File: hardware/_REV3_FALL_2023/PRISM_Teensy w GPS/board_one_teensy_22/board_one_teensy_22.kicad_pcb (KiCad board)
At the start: 2 copper layers, 61 x 88.9 mm, 32 parts, among them J1 Micro_SD_Card_Det_Hirose_DM3AT, J3 3387, Q1 AO3400A, Q2 AO3400A, U1 Teensy4.0, U2 GPS-14414, U3 3966, U4 RFM69HCW_Breakout, U5 CT25E-16T150-1, U6 CMI-9605-1280T

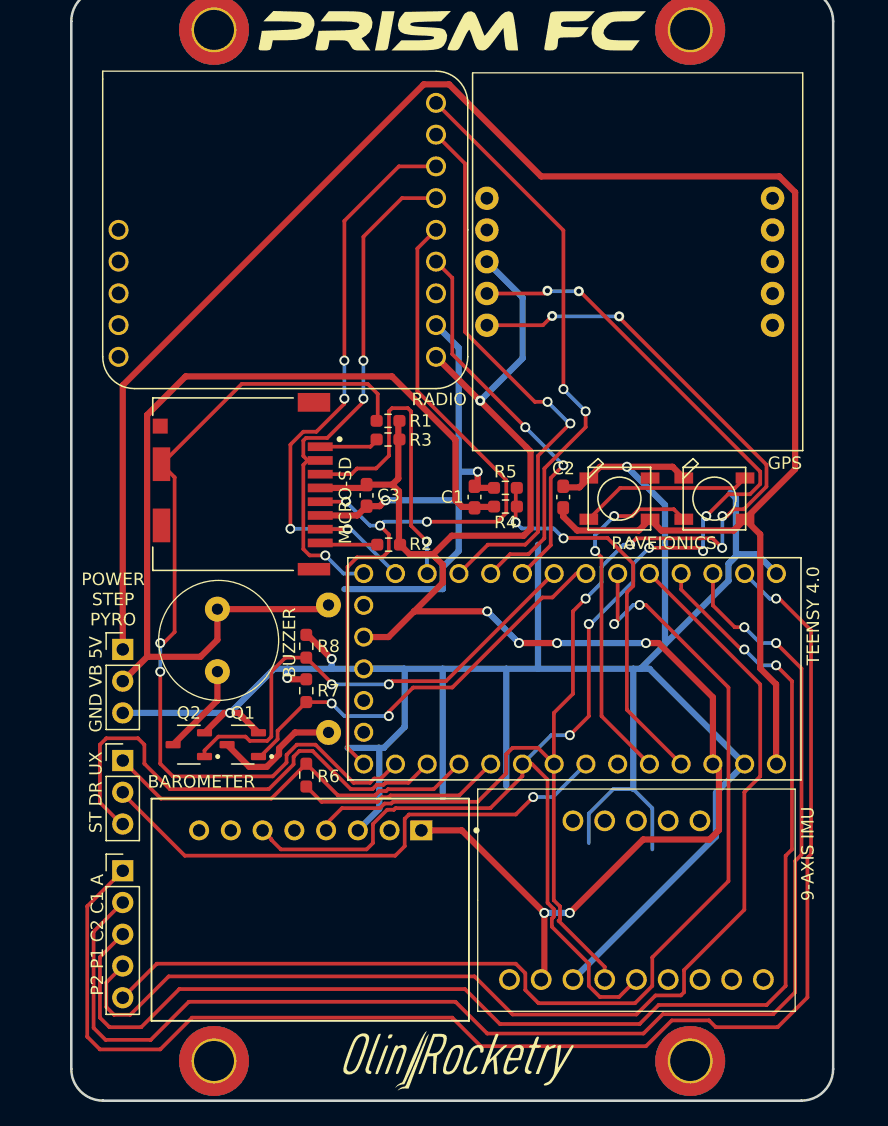
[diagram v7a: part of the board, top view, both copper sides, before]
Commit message: Added 3.3V line and fixed analog routing issues on Teensy
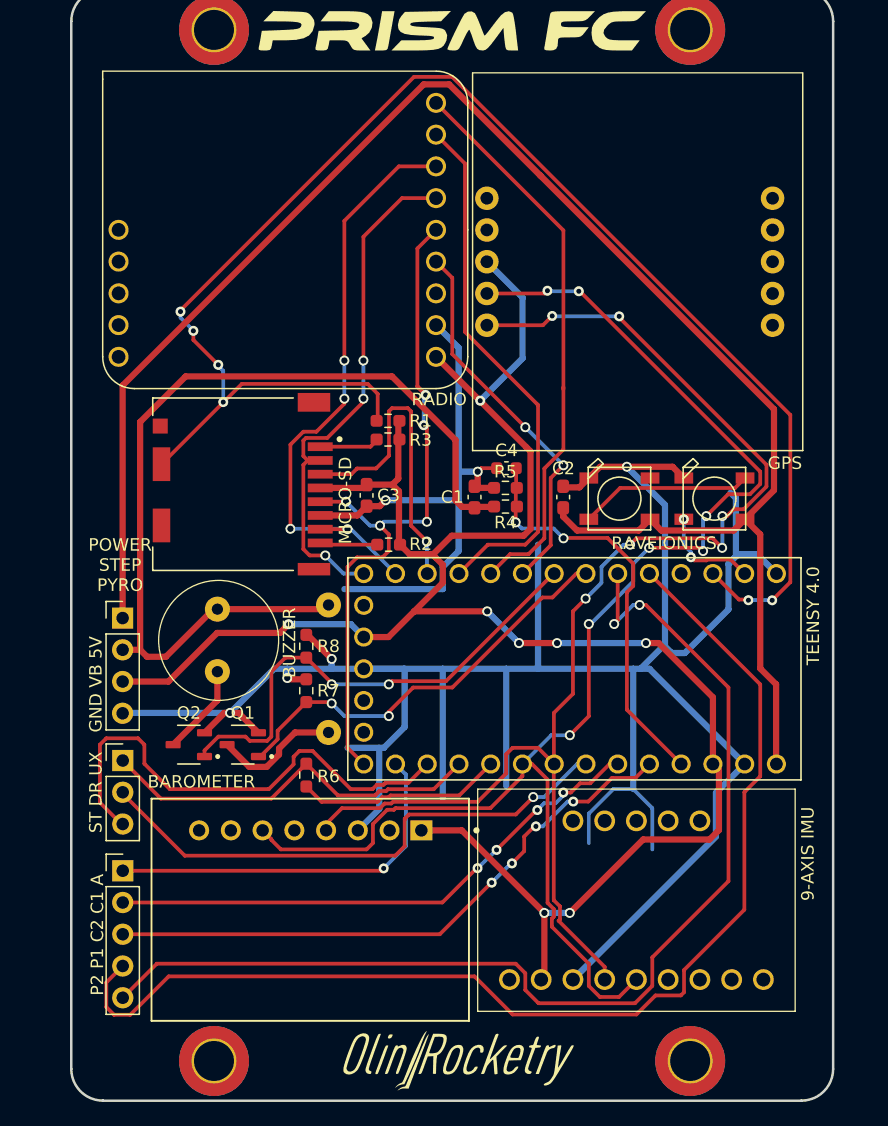
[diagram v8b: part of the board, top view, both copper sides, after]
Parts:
- added C4: 10uf, Capacitor_SMD:C_0603_1608Metric, F.Cu at (142.0, 88.4)
- Power1: value Conn_01x03_Socket -> Conn_01x04_Socket; footprint Connector_PinHeader_2.54mm:PinHeader_1x03_P2.54mm_Vertical -> Connector_PinHeader_2.54mm:PinHeader_1x04_P2.54mm_Vertical
- moved Power1 2.51 mm to (111.3, 100.4)
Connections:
- Power1 pad 3: GND -> /3.3V
- Pyro1 pad 1: /ARM -> /CONT 2
- Pyro1 pad 3: /CONT 2 -> /ARM
- U1 pad 0: /ARM -> /NEOPIXEL
- U1 pad 1: /CONT 1 -> /SD_DETECT
- U1 pad 14: /SD_DETECT -> /CONT 2
- U1 pad 2: /CONT 2 -> unconnected-(U1-Pad2)
- U1 pad 21: unconnected-(U1-Pad21) -> /CONT 1
- U1 pad 22: /NEOPIXEL -> /ARM
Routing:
- net /CONT 2: track 104.1 -> 30.3 mm, vias 2 -> 1
- net /ARM: track 113.2 -> 48.5 mm, vias 1 -> 4
- net /CONT 1: track 109.1 -> 44.7 mm, vias 2 -> 4
- net /SD_DETECT: track 70.0 -> 120.6 mm, vias 2 -> 6
- net /3.3V: track 141.5 -> 163.1 mm, vias 7 -> 8
- net /NEOPIXEL: track 28.4 -> 8.17 mm
- net /5V: track 153.8 -> 138.9 mm
- net /SD_SCK: track 64.8 -> 57.3 mm, vias 3 -> 5
- net GND: track 255.4 -> 258.9 mm
- net /CS 1: track 45.7 -> 42.9 mm, vias 2 -> 0
- net /VBAT: track 76.0 -> 73.7 mm
- net /V_Mon: track 31.6 -> 33.1 mm
- net /Radio_RST: track 46.6 -> 45.3 mm, vias 2 -> 0
